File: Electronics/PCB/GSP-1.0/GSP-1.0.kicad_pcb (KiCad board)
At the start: 2 copper layers, 150 x 60 mm, 12 parts, among them SW1 SW_Push, SW10 SW_Push, SW2 SW_Push, SW3 SW_Push, SW4 SW_Push, SW5 SW_Push, SW6 SW_Push, SW7 SW_Push, SW8 SW_Push, SW9 SW_Push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

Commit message: Fix ESP32 version
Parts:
- removed U3: ESP32-WROOM-32, RF_Module:ESP32-WROOM-32
- added BZ1: Buzzer1, Buzzer_Beeper:Buzzer_12x9.5RM7.6, F.Cu at (103.0, 126.0)
- added Q1: ASS8050-L-HF, Package_TO_SOT_SMD:SOT-23, B.Cu at (194.0, 83.0)
- added Q2: ASS8050-L-HF, Package_TO_SOT_SMD:SOT-23, F.Cu at (203.0, 83.0)
- added RV_buzzer1: R_Buzzer1, Potentiometer_THT:Potentiometer_Alps_RK09K_Single_Horizontal, F.Cu at (214.0, 122.0)
- added SW_PWR1: SW_SPST, GustavsGlobalLibrary:Slide-SW-GF-1123-1110, F.Cu at (88.0, 125.4)
- added U1: ESP32-S2-WROOM-I, GustavsGlobalLibrary:XCVR_ESP32-S2-WROOM-I, B.Cu at (150.0, 100.0)
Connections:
- SW1 pad 2: unconnected-(SW1-Pad2) -> GNDREF
- SW2 pad 2: unconnected-(SW2-Pad2) -> GNDREF
- SW3 pad 2: unconnected-(SW3-Pad2) -> GNDREF
- SW4 pad 2: unconnected-(SW4-Pad2) -> GNDREF
- SW5 pad 2: unconnected-(SW5-Pad2) -> GNDREF
- SW6 pad 2: unconnected-(SW6-Pad2) -> GNDREF
- SW7 pad 2: unconnected-(SW7-Pad2) -> GNDREF
- SW8 pad 2: unconnected-(SW8-Pad2) -> GNDREF
- U2 pad DC: Net-(U3-Pad16) -> /IO8
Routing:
- net GNDREF: track 114.6 -> 0.00 mm
- net Net-(U3-Pad16): track 64.3 -> 0.00 mm
- net Net-(U2-PadRES): track 47.4 -> 0.00 mm
- net +3V3: track 46.0 -> 0.00 mm, vias 1 -> 0
- net Net-(U2-PadSCL): track 26.8 -> 0.00 mm
- net Net-(U2-PadSDA): track 25.8 -> 0.00 mm

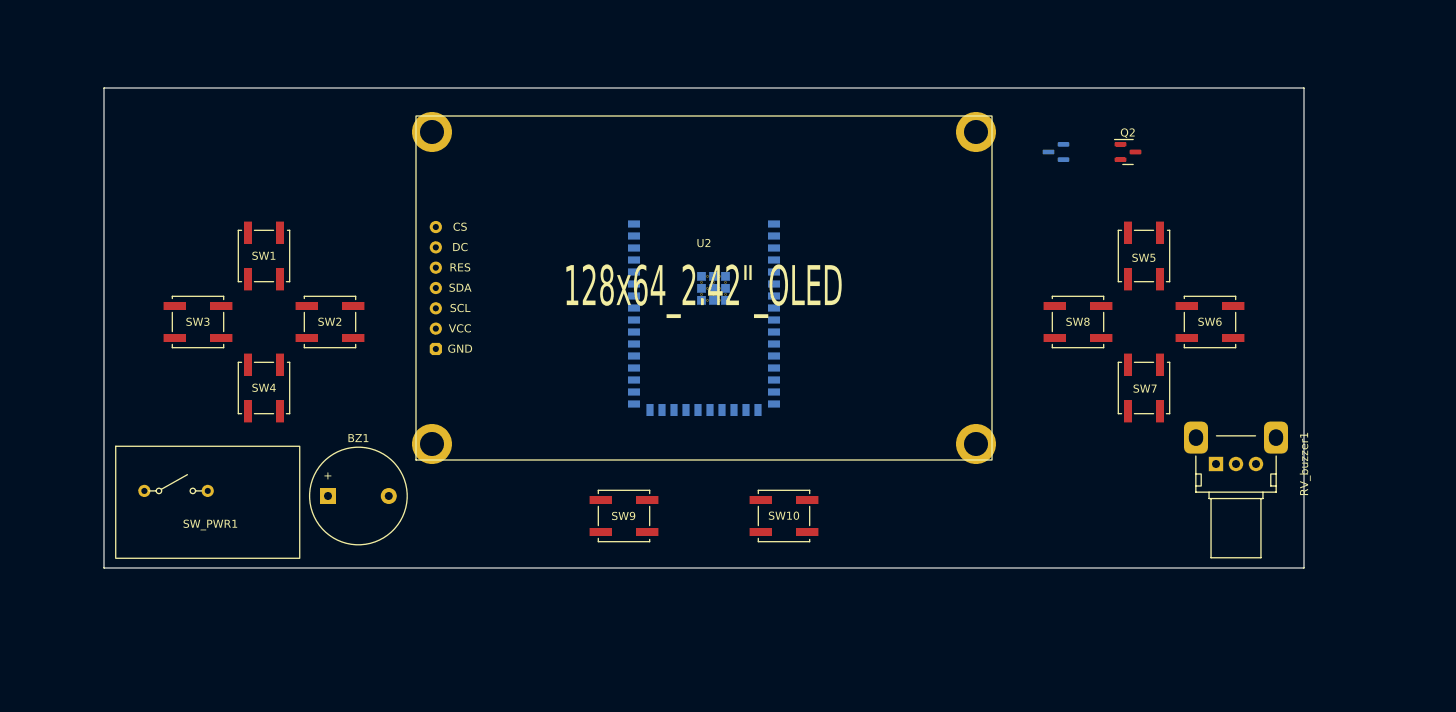
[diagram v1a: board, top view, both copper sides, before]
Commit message: PCB almost finished, but lots of errors
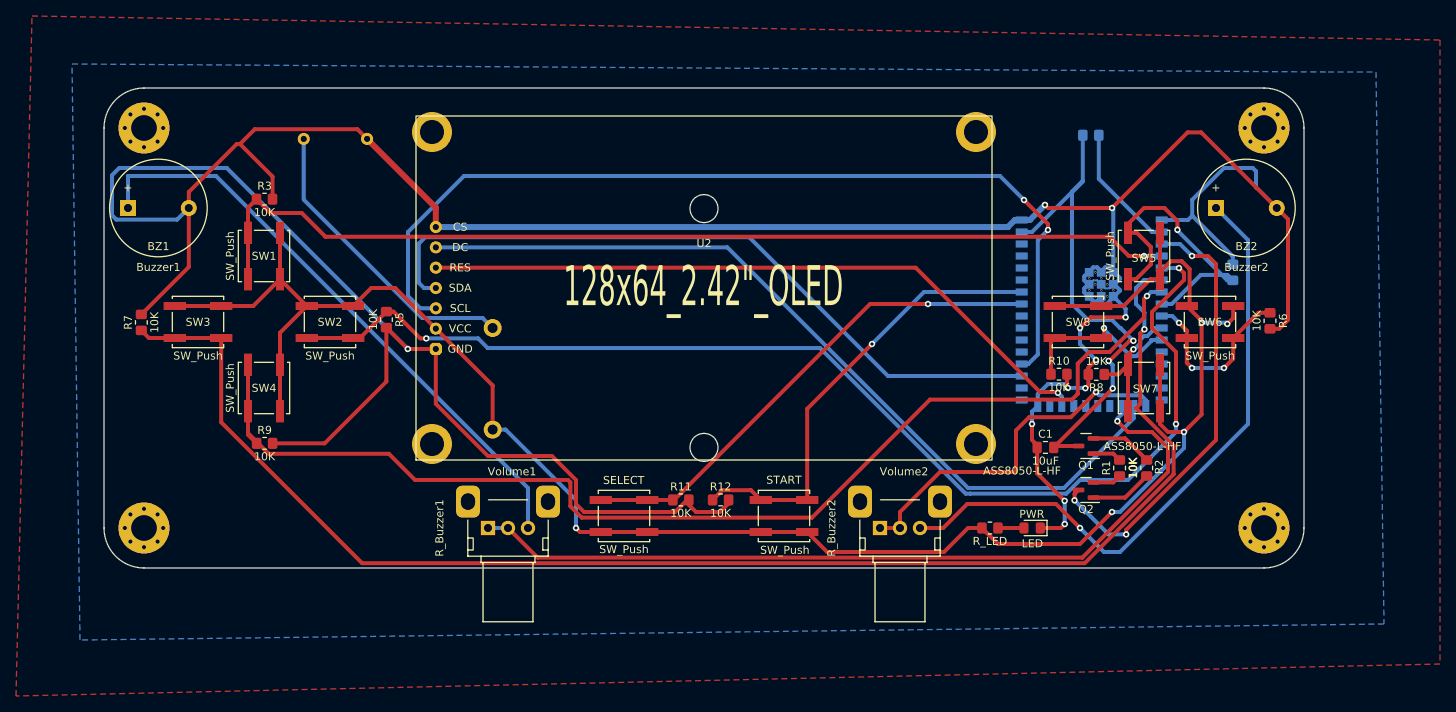
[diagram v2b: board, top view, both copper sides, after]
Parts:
- added BT1: Battery_pack, GustavsGlobalLibrary:3xAA holder (534-2464), B.Cu at (150.0, 105.0)
- added BZ2: Buzzer2, Buzzer_Beeper:Buzzer_12x9.5RM7.6, F.Cu at (214.0, 90.0)
- added C1: 10uF, Capacitor_SMD:C_0805_2012Metric_Pad1.18x1.45mm_HandSolder, F.Cu at (192.7, 119.9)
- added EN_Pull-up1: 10K, Resistor_SMD:R_0805_2012Metric_Pad1.20x1.40mm_HandSolder, B.Cu at (198.3, 80.9)
- added PWR: LED, LED_SMD:LED_0805_2012Metric_Pad1.15x1.40mm_HandSolder, F.Cu at (191.0, 130.0)
- added R1: 10K, Resistor_SMD:R_0805_2012Metric_Pad1.20x1.40mm_HandSolder, F.Cu at (201.9, 122.5)
- added R10: 10K, Resistor_SMD:R_0805_2012Metric_Pad1.20x1.40mm_HandSolder, F.Cu at (194.4, 110.8)
- added R11: 10K, Resistor_SMD:R_0805_2012Metric_Pad1.20x1.40mm_HandSolder, F.Cu at (147.1, 126.5)
- added R12: 10K, Resistor_SMD:R_0805_2012Metric_Pad1.20x1.40mm_HandSolder, F.Cu at (152.1, 126.5)
- added R2: 10K, Resistor_SMD:R_0805_2012Metric_Pad1.20x1.40mm_HandSolder, F.Cu at (205.3, 122.5)
- added R3: 10K, Resistor_SMD:R_0805_2012Metric_Pad1.20x1.40mm_HandSolder, F.Cu at (95.1, 88.9)
- added R4: 10K, Resistor_SMD:R_0805_2012Metric_Pad1.20x1.40mm_HandSolder, B.Cu at (216.1, 98.0)
- added R5: 10K, Resistor_SMD:R_0805_2012Metric_Pad1.20x1.40mm_HandSolder, F.Cu at (110.3, 104.0)
- added R6: 10K, Resistor_SMD:R_0805_2012Metric_Pad1.20x1.40mm_HandSolder, F.Cu at (220.8, 104.1)
- added R7: 10K, Resistor_SMD:R_0805_2012Metric_Pad1.20x1.40mm_HandSolder, F.Cu at (79.7, 104.3)
- added R8: 10K, Resistor_SMD:R_0805_2012Metric_Pad1.20x1.40mm_HandSolder, F.Cu at (199.0, 110.8)
- added R9: 10K, Resistor_SMD:R_0805_2012Metric_Pad1.20x1.40mm_HandSolder, F.Cu at (95.1, 119.4)
- added REF**: MountingHole_3.2mm_M3_Pad_Via, MountingHole:MountingHole_3.2mm_M3_Pad_Via, F.Cu at (220.0, 130.0)
- added REF**: MountingHole_3.2mm_M3_Pad_Via, MountingHole:MountingHole_3.2mm_M3_Pad_Via, F.Cu at (220.0, 80.0)
- added REF**: MountingHole_3.2mm_M3_Pad_Via, MountingHole:MountingHole_3.2mm_M3_Pad_Via, F.Cu at (80.0, 80.0)
- added REF**: MountingHole_3.2mm_M3_Pad_Via, MountingHole:MountingHole_3.2mm_M3_Pad_Via, F.Cu at (80.0, 130.0)
- added R_LED1: R_LED, Resistor_SMD:R_0805_2012Metric_Pad1.20x1.40mm_HandSolder, F.Cu at (185.7, 130.0)
- added Volume2: R_Buzzer2, Potentiometer_THT:Potentiometer_Alps_RK09K_Single_Horizontal, F.Cu at (172.0, 130.0)
- Q1: moved to F.Cu
- SW_PWR1: moved to B.Cu
- moved Volume1 91.4 mm to (123.0, 130.0)
- moved U1 48.5 mm to (198.5, 99.5)
- moved SW_PWR1 45.6 mm to (100.0, 81.4), turned to 180 degrees
- moved BZ1 43.8 mm to (78.0, 90.0)
- moved Q2 42.6 mm to (197.8, 125.2), turned to 180 degrees
- moved Q1 36.9 mm to (197.8, 119.8)
- renumbered SW9 to SELECT, SW10 to START, RV_buzzer1 to Volume1
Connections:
- SELECT pad 1: unconnected-(SW9-Pad1) -> /SELECT
- SELECT pad 2: unconnected-(SW9-Pad2) -> +3V3
- START pad 1: unconnected-(SW10-Pad1) -> /START
- START pad 2: unconnected-(SW10-Pad2) -> +3V3
- SW1 pad 1: unconnected-(SW1-Pad1) -> /IO1
- SW1 pad 2: GNDREF -> +3V3
- SW2 pad 1: unconnected-(SW2-Pad1) -> /IO2
- SW2 pad 2: GNDREF -> +3V3
- SW3 pad 1: unconnected-(SW3-Pad1) -> /IO3
- SW3 pad 2: GNDREF -> +3V3
- SW4 pad 1: unconnected-(SW4-Pad1) -> /IO4
- SW4 pad 2: GNDREF -> +3V3
- SW5 pad 1: unconnected-(SW5-Pad1) -> /IO5
- SW5 pad 2: GNDREF -> +3V3
- SW6 pad 1: unconnected-(SW6-Pad1) -> /IO6
- SW6 pad 2: GNDREF -> +3V3
- SW7 pad 1: unconnected-(SW7-Pad1) -> /IO7
- SW7 pad 2: GNDREF -> +3V3
- SW8 pad 1: unconnected-(SW8-Pad1) -> /IO8
- SW8 pad 2: GNDREF -> +3V3
- U1 pad 10: unconnected-(U1-Pad10) -> /IO7
- U1 pad 17: unconnected-(U1-Pad17) -> /BUZZER_PIN2
- U1 pad 18: unconnected-(U1-Pad18) -> /IO15
- U1 pad 35: unconnected-(U1-Pad35) -> /SELECT
- U1 pad 36: unconnected-(U1-Pad36) -> /START
- U1 pad 4: unconnected-(U1-Pad4) -> /IO1
- U1 pad 5: unconnected-(U1-Pad5) -> /IO2
- U1 pad 6: unconnected-(U1-Pad6) -> /IO3
- U1 pad 7: unconnected-(U1-Pad7) -> /IO4
- U1 pad 8: unconnected-(U1-Pad8) -> /IO5
- U1 pad 9: unconnected-(U1-Pad9) -> /IO6
- U2 pad DC: /IO8 -> /IO15
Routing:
- net GNDREF: track 0.00 -> 453.2 mm, vias 0 -> 11
- net +3V3: track 0.00 -> 259.0 mm, vias 0 -> 5
- net /IO3: track 0.00 -> 181.6 mm, vias 0 -> 1
- net /IO4: track 0.00 -> 154.4 mm, vias 0 -> 1
- net /IO2: track 0.00 -> 148.4 mm, vias 0 -> 3
- net /IO1: track 0.00 -> 126.5 mm, vias 0 -> 1
- net Net-(U1-Pad30): track 0.00 -> 116.8 mm, vias 0 -> 2
- net /IO15: track 0.00 -> 104.8 mm
- net /BUZZER_PIN: track 0.00 -> 103.8 mm, vias 0 -> 1
- net Net-(U1-Pad29): track 0.00 -> 90.2 mm
- net Net-(U1-Pad24): track 0.00 -> 86.1 mm, vias 0 -> 1
- net Net-(Volume2-Pad3): track 0.00 -> 80.0 mm, vias 0 -> 1
- net Net-(BZ1-Pad1): track 0.00 -> 75.2 mm
- net /EN: track 0.00 -> 62.9 mm, vias 0 -> 3
- net /SELECT: track 0.00 -> 62.8 mm, vias 0 -> 1
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- added copper zone on F.Cu, net +3V3
- added copper zone on B.Cu, net GNDREF
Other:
- outline, holes or cut-outs redrawn

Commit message: Fix PCB
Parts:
- added C2: 22uF, Capacitor_SMD:C_0805_2012Metric_Pad1.18x1.45mm_HandSolder, B.Cu at (137.0, 111.0)
- added C3: 0.1uF, Capacitor_SMD:C_0805_2012Metric_Pad1.18x1.45mm_HandSolder, B.Cu at (142.1, 111.0)
- added G***: LOGO, LOGO, F.Cu at (87.0, 130.0)
- added G***: LOGO, LOGO, F.Cu at (212.0, 130.0)
- added J1: USB_C_Receptacle_USB2.0, Connector_USB:USB_C_Receptacle_HRO_TYPE-C-31-M-12, B.Cu at (150.0, 130.8)
- added J_EN1: Conn_01x01_Male, Connector_PinHeader_1.27mm:PinHeader_1x01_P1.27mm_Vertical, F.Cu at (150.4, 76.7)
- added J_IO_1: Conn_01x01_Male, Connector_PinHeader_1.27mm:PinHeader_1x01_P1.27mm_Vertical, F.Cu at (221.4, 122.0)
- added J_UART1: Conn_01x06_Male, Connector_PinHeader_1.27mm:PinHeader_1x06_P1.27mm_Vertical, F.Cu at (220.2, 110.7)
- added R13: 5.1K, Resistor_SMD:R_0805_2012Metric_Pad1.20x1.40mm_HandSolder, F.Cu at (152.7, 115.0)
- added R14: 5.1K, Resistor_SMD:R_0805_2012Metric_Pad1.20x1.40mm_HandSolder, B.Cu at (147.0, 115.0)
- added U3: AZ1117-3.3, Package_TO_SOT_SMD:SOT-223-3_TabPin2, B.Cu at (130.6, 112.8)
- added U4: AZ1117-3.3, Package_TO_SOT_SMD:SOT-223-3_TabPin2, B.Cu at (160.8, 112.8)
- D_3V3: renamed from PWR; value LED -> PWR
- SELECT1: renamed from SELECT; value SW_Push -> SELECT
- START1: renamed from START; value SW_Push -> START
- moved R11 3.00 mm to (147.1, 123.5)
- moved R12 3.00 mm to (152.1, 123.5)
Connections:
- BT1 pad 1: +3V3 -> Net-(BT1-Pad1)
- U1 pad 22: unconnected-(U1-Pad22) -> /D-
- U1 pad 23: unconnected-(U1-Pad23) -> /D+
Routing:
- net /TX: track 0.00 -> 84.2 mm, vias 0 -> 1
- net /RX: track 0.00 -> 80.1 mm, vias 0 -> 2
- net GNDREF: track 453.2 -> 514.8 mm, vias 11 -> 14
- net +3V3: track 259.0 -> 317.6 mm, vias 5 -> 10
- net /D-: track 0.00 -> 56.1 mm, vias 0 -> 2
- net /D+: track 0.00 -> 54.6 mm, vias 0 -> 2
- net /EN: track 62.9 -> 114.2 mm
- net /DTR: track 3.59 -> 36.2 mm, vias 0 -> 2
- net +5V: track 0.00 -> 20.8 mm, vias 0 -> 2
- net /RTS: track 7.77 -> 26.5 mm, vias 0 -> 2
- net /IO_0: track 56.0 -> 72.0 mm
- net Net-(J1-PadA5): track 0.00 -> 15.4 mm, vias 0 -> 1
- net Net-(J1-PadB5): track 0.00 -> 11.9 mm
- net /SELECT: track 62.8 -> 70.7 mm
- net Net-(BT1-Pad1): track 0.00 -> 5.45 mm
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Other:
- board text added: "1.0"
- board text added: "G. Abrahamsson 2022"
- board text added: "GSP"
- board text added: "Gamestation Portable 1.0"
- board text added: "RTS DTR RX TX 3V3 GND"
- board text added: "SSD1309"

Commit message: +
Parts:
- added REF**: KiCad-Logo2_5mm_SilkScreen, Symbol:KiCad-Logo2_5mm_SilkScreen, F.Cu at (83.0, 120.0)

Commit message: Update PCB
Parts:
- moved J_EN1 42.7 mm to (192.9, 81.2)
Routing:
- net /EN: track 114.2 -> 70.5 mm
- net GNDREF: track 514.8 -> 513.5 mm
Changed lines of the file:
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@@
   )
   (footprint "Connector_PinHeader_1.27mm:PinHeader_1x01_P1.27mm_Vertical" (layer "F.Cu")
-    (at 150.36 76.7)
+    (at 192.86 81.2)
     (descr "Through hole straight pin header, 1x01, 1.27mm pitch, single row")
     (tags "Through hole pin header THT 1x01 1.27mm single row")
@@
       (effects (font (size 1 1) (thickness 0.15)))
     )
-    (fp_text value "5.1K" (at 0 1.65) (layer "F.Fab")
+    (fp_text value "5.1K" (at 0 1.65) (layer "F.SilkS")
       (effects (font (size 1 1) (thickness 0.15)))
     )
@@
       (effects (font (size 1 1) (thickness 0.15)) (justify mirror))
     )
-    (fp_text value "5.1K" (at 0 -1.65) (layer "B.Fab")
+    (fp_text value "5.1K" (at 0 -1.65) (layer "B.SilkS")
       (effects (font (size 1 1) (thickness 0.15)) (justify mirror))
     )
@@
   (segment (start 201.283844 101.048038) (end 201.157708 101.048038) (width 0.5) (layer "B.Cu") (net 1))
   (segment (start 131 119) (end 132.9 117.1) (width 0.5) (layer "B.Cu") (net 1))
-  (segment (start 119.068064 92.208064) (end 150.891649 92.208064) (width 0.75) (layer "B.Cu") (net 1))
   (segment (start 199.164323 97.428517) (end 199.657708 97.921902) (width 0.5) (layer "B.Cu") (net 1))
   (segment (start 145.68 131.87) (end 145.68 127.69) (width 0.5) (layer "B.Cu") (net 1))
@@
   (segment (start 145.97 119.72) (end 145.97 114.98) (width 0.5) (layer "B.Cu") (net 1))
   (segment (start 199.164323 101.667559) (end 198.651093 101.667559) (width 0.5) (layer "B.Cu") (net 1))
-  (segment (start 152.099713 91) (end 189.21967 91) (width 0.75) (layer "B.Cu") (net 1))
   (segment (start 219 85.4) (end 218.6 85) (width 0.5) (layer "B.Cu") (net 1))
   (segment (start 198.031572 98.048038) (end 198.157708 98.048038) (width 0.5) (layer "B.Cu") (net 1))
-  (segment (start 150.891649 92.208064) (end 152.099713 91) (width 0.75) (layer "B.Cu") (net 1))
+  (segment (start 152.5 92.5) (end 153.501962 91.498038) (width 0.75) (layer "B.Cu") (net 1))
   (segment (start 201.157708 101.048038) (end 201.157708 101.174174) (width 0.5) (layer "B.Cu") (net 1))
   (segment (start 202.706654 103.66566) (end 202.706654 102.596984) (width 0.5) (layer "B.Cu") (net 1))
@@
   (segment (start 202.706654 102.596984) (end 201.157708 101.048038) (width 0.5) (layer "B.Cu") (net 1))
   (segment (start 218.6 85) (end 215 85) (width 0.5) (layer "B.Cu") (net 1))
+  (segment (start 116.48 92.38) (end 116.6 92.5) (width 0.75) (layer "B.Cu") (net 1))
   (segment (start 194.988725 112) (end 195.475023 112.486298) (width 0.5) (layer "B.Cu") (net 1))
   (segment (start 201.157708 101.174174) (end 200.331882 102) (width 0.5) (layer "B.Cu") (net 1))
@@
   (segment (start 193 112) (end 194.988725 112) (width 0.5) (layer "B.Cu") (net 1))
   (segment (start 76.909752 85) (end 76 85.909752) (width 0.5) (layer "B.Cu") (net 1))
+  (segment (start 153.501962 91.498038) (end 189.717708 91.498038) (width 0.75) (layer "B.Cu") (net 1))
   (segment (start 145.68 127.69) (end 145.835 127.69) (width 0.5) (layer "B.Cu") (net 1))
   (segment (start 191.717708 113.282292) (end 193 112) (width 0.5) (layer "B.Cu") (net 1))
   (segment (start 145.05601 114.98) (end 142.083426 112.007416) (width 0.5) (layer "B.Cu") (net 1))
-  (segment (start 117.86 91) (end 119.068064 92.208064) (width 0.75) (layer "B.Cu") (net 1))
   (segment (start 198.157708 101.174174) (end 198.157708 101.048038) (width 0.5) (layer "B.Cu") (net 1))
   (segment (start 219 87.4) (end 219 85.4) (width 0.5) (layer "B.Cu") (net 1))
@@
   (segment (start 163.15 115.94) (end 163.15 113.15) (width 0.5) (layer "B.Cu") (net 1))
   (segment (start 210.501962 91.498038) (end 211.03 90.97) (width 0.5) (layer "B.Cu") (net 1))
-  (segment (start 189.21967 91) (end 189.717708 91.498038) (width 0.75) (layer "B.Cu") (net 1))
   (segment (start 202 98.764194) (end 202 98.831882) (width 0.5) (layer "B.Cu") (net 1))
+  (segment (start 116.6 92.5) (end 152.5 92.5) (width 0.75) (layer "B.Cu") (net 1))
   (segment (start 199.657708 101.174174) (end 199.164323 101.667559) (width 0.5) (layer "B.Cu") (net 1))
   (segment (start 200.663187 100.042559) (end 201.157708 99.548038) (width 0.25) (layer "B.Cu") (net 1))
@@
   (segment (start 76 90.899022) (end 76.550489 91.449511) (width 0.5) (layer "B.Cu") (net 1))
   (segment (start 197.538187 100.554653) (end 197.538187 100.041423) (width 0.5) (layer "B.Cu") (net 1))
-  (segment (start 116.48 92.38) (end 117.86 91) (width 0.75) (layer "B.Cu") (net 1))
   (segment (start 165.4 133) (end 162.9 130.5) (width 0.5) (layer "F.Cu") (net 2))
   (segment (start 219 109.349502) (end 219 111.196389) (width 0.5) (layer "F.Cu") (net 2))
@@
   (via (at 200.573747 109.116155) (size 0.8) (drill 0.4) (layers "F.Cu" "B.Cu") (net 16))
   (via (at 201.08952 112.55798) (size 0.8) (drill 0.4) (layers "F.Cu" "B.Cu") (net 16))
-  (segment (start 150.36 76.7) (end 193.14 76.7) (width 0.25) (layer "B.Cu") (net 16))
+  (segment (start 197.06 81.2) (end 197.35 80.91) (width 0.25) (layer "B.Cu") (net 16))
   (segment (start 197.35 80.91) (end 197.35 86.65) (width 0.5) (layer "B.Cu") (net 16))
   (segment (start 198 104) (end 196 102) (width 0.5) (layer "B.Cu") (net 16))
@@
   (segment (start 203.671524 106.597922) (end 202.073602 105) (width 0.5) (layer "B.Cu") (net 16))
   (segment (start 202.073602 105) (end 202 105) (width 0.5) (layer "B.Cu") (net 16))
-  (segment (start 193.14 76.7) (end 197.35 80.91) (width 0.25) (layer "B.Cu") (net 16))
+  (segment (start 192.5 81.2) (end 197.06 81.2) (width 0.25) (layer "B.Cu") (net 16))
   (segment (start 196 102) (end 196 88) (width 0.5) (layer "B.Cu") (net 16))
   (segment (start 201.08952 112.55798) (end 201.08952 109.631928) (width 0.5) (layer "B.Cu") (net 16))

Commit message: Final 1.0 version with PCB ordered
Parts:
- removed the REF** at (83.0, 120.0)
- added C4: 10uF, Capacitor_SMD:C_0805_2012Metric_Pad1.18x1.45mm_HandSolder, F.Cu at (120.0, 113.5)
- added C5: 10uF, Capacitor_SMD:C_0805_2012Metric_Pad1.18x1.45mm_HandSolder, B.Cu at (140.0, 120.0)
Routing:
- net +5V: track 20.8 -> 43.3 mm
- net GNDREF: track 513.5 -> 523.1 mm
- net Net-(BT1-Pad1): track 5.45 -> 10.3 mm
